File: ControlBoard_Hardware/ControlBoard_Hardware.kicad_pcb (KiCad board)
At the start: 2 copper layers, 141.5 x 46.2 mm, 24 parts, among them U2 TSR_1-2450

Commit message: updatedfor final report
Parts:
- added Conn13: Molex_SL_02, MRDT_Connectors:MOLEX_SL_02_Horizontal, F.Cu at (152.4, 68.6)
- Conn4: value Molex_SL_07 -> Molex_SL_02; footprint MRDT_Connectors:MOLEX_SL_07_Horizontal -> MRDT_Connectors:MOLEX_SL_02_Horizontal
- Conn5: value Molex_SL_07 -> Molex_SL_03; footprint MRDT_Connectors:MOLEX_SL_07_Horizontal -> MRDT_Connectors:MOLEX_SL_03_Horizontal
- moved Conn5 9.14 mm to (133.1, 68.6)
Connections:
- net Discharge2 renamed SERVO
- Conn10 pad 1: +5V -> +3V3
- Conn10 pad 2: +5V -> +3V3
- Conn11 pad 1: +5V -> +3V3
- Conn11 pad 2: +5V -> +3V3
- Conn12 pad 1: +5V -> +3V3
- Conn12 pad 2: +5V -> +3V3
- Conn3 pad 1: +5V -> +3V3
- Conn3 pad 2: +5V -> +3V3
- Conn4 pad 2: Charge2 -> Discharge1
- Conn5 pad 1: Discharge1 -> +5V
- Conn5 pad 3: Discharge3 -> GND
- Conn6 pad 1: +5V -> +3V3
- Conn6 pad 2: +5V -> +3V3
- Conn7 pad 1: +3V3 -> Trigger Signal
- Conn7 pad 2: Trigger Signal -> GND
- Conn8 pad 1: +5V -> +3V3
- Conn8 pad 2: +5V -> +3V3
- Conn9 pad 1: +5V -> +3V3
- Conn9 pad 2: +5V -> +3V3
- U1 pad 10: Discharge6 -> unconnected-(U1-CS-Pad10)
- U1 pad 11: Discharge7 -> unconnected-(U1-MOSI-Pad11)
- U1 pad 14: Charge2 -> unconnected-(U1-A0-Pad14)
- U1 pad 15: Charge3 -> unconnected-(U1-A1-Pad15)
- U1 pad 16: Charge4 -> unconnected-(U1-A2-Pad16)
- U1 pad 2: Charge5 -> unconnected-(U1-OUT2-Pad2)
- U1 pad 3: Charge6 -> unconnected-(U1-LRCLK2-Pad3)
- U1 pad 4: Charge7 -> unconnected-(U1-BCLK2-Pad4)
- U1 pad 7: Discharge3 -> unconnected-(U1-RX2-Pad7)
- U1 pad 8: Discharge4 -> unconnected-(U1-TX2-Pad8)
- U1 pad 9: Discharge5 -> unconnected-(U1-OUT1C-Pad9)
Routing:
- net +5V: track 77.4 -> 175.4 mm
- net Charge5: track 78.7 -> 0.00 mm
- net Charge6: track 73.1 -> 0.00 mm
- net Charge7: track 67.6 -> 0.00 mm
- net Charge3: track 62.7 -> 0.00 mm, vias 1 -> 0
- net Charge4: track 62.7 -> 0.00 mm, vias 1 -> 0
- net Charge2: track 62.7 -> 0.00 mm, vias 1 -> 0
- net +3V3: track 120.7 -> 60.0 mm, vias 0 -> 1
- net Discharge3: track 46.1 -> 0.00 mm
- net Discharge4: track 40.6 -> 0.00 mm
- net Discharge5: track 35.1 -> 0.00 mm
- net Discharge6: track 29.6 -> 0.00 mm
- net Discharge7: track 24.1 -> 0.00 mm
- net Discharge1: track 57.1 -> 75.0 mm
- net LCD_TX: track 118.1 -> 101.1 mm, vias 0 -> 1
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- added copper zone on F.Cu, net +3V3
- removed copper zone on F.Cu, net +5V
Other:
- board text added: "Charge/Discharge"
- board text added: "Safety Switch"
- board text added: "Servo"
- board text removed: "Charging Circuits"
- board text removed: "Discharge Circuits"

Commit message: started layout
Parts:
- removed D3: LED, LED_SMD:LED_0603_1608Metric_Pad1.05x0.95mm_HandSolder
- removed R3: 100, Resistor_SMD:R_0603_1608Metric_Pad0.98x0.95mm_HandSolder
- added Conn14: Molex_SL_02, MRDT_Connectors:MOLEX_SL_02_Horizontal, F.Cu at (215.9, 100.3)
- added PowerSwich1: Molex_SL_02, MRDT_Connectors:MOLEX_SL_02_Horizontal, F.Cu at (69.8, 100.3)
- Conn10, Conn11, Conn3, Conn6, Conn8, Conn9: value Molex_SL_05 -> Molex_SL_02; footprint MRDT_Connectors:MOLEX_SL_05_Horizontal -> MRDT_Connectors:MOLEX_SL_02_Horizontal
- Conn12: value Molex_SL_05 -> Molex_SL_03; footprint MRDT_Connectors:MOLEX_SL_05_Horizontal -> MRDT_Connectors:MOLEX_SL_03_Horizontal
- H1, H2, H3, H4: footprint MRDT_Drill_Holes:4_40_Hole_Corner -> MountingHole:MountingHole_3.2mm_M3
- moved H3 188.7 mm to (282.1, 43.1), turned to 0 degrees
- moved H2 184.1 mm to (282.1, 35.1), turned to 0 degrees
- moved Conn1 162.1 mm to (59.7, 100.3), turned to 0 degrees
- moved Conn4 111.3 mm to (226.1, 100.3)
- moved H1 87.2 mm to (282.1, 27.2), turned to 0 degrees
- moved Conn2 83.5 mm to (181.6, 100.3)
- moved D2 77.5 mm to (178.0, 127.0), turned to 0 degrees
- moved R2 76.3 mm to (182.3, 126.9), turned to 0 degrees
- moved U1 74.6 mm to (138.2, 124.8), turned to 0 degrees
- moved D1 73.2 mm to (178.0, 124.4), turned to 0 degrees
- moved R1 72.1 mm to (182.3, 124.4), turned to 0 degrees
- moved Conn11 69.0 mm to (134.6, 100.3), turned to 0 degrees
- moved U2 67.3 mm to (177.8, 118.1)
- moved Conn10 61.5 mm to (124.5, 100.3), turned to 0 degrees
- moved Conn9 54.0 mm to (114.3, 100.3), turned to 0 degrees
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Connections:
- net Charge1 renamed Charge
- Conn1 pad 2: Input_PWR -> Net-(Conn1-Pad2)
- Conn10 pad 1: +3V3 -> Coil5
- Conn10 pad 2: +3V3 -> GND
- Conn11 pad 1: +3V3 -> Coil6
- Conn11 pad 2: +3V3 -> GND
- Conn12 pad 1: +3V3 -> +5V
- Conn12 pad 2: +3V3 -> LED Data
- Conn12 pad 3: Sensor7 -> GND
- Conn3 pad 1: +3V3 -> Coil1
- Conn3 pad 2: +3V3 -> GND
- Conn4 pad 2: Discharge1 -> GND
- Conn6 pad 1: +3V3 -> Coil2
- Conn6 pad 2: +3V3 -> GND
- Conn8 pad 1: +3V3 -> Coil3
- Conn8 pad 2: +3V3 -> GND
- Conn9 pad 1: +3V3 -> Coil4
- Conn9 pad 2: +3V3 -> GND
- U1 pad 17: Sensor1 -> unconnected-(U1-A3-Pad17)
- U1 pad 18: Sensor2 -> Coil6
- U1 pad 19: Sensor3 -> Coil5
- U1 pad 20: Sensor4 -> Coil4
- U1 pad 21: Sensor5 -> Coil3
- U1 pad 22: Sensor6 -> Coil2
- U1 pad 23: Sensor7 -> Coil1
- U1 pad 5: Discharge1 -> Discharge
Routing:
- net +5V: track 175.4 -> 0.00 mm
- net LCD_TX: track 101.1 -> 0.00 mm, vias 1 -> 0
- net LCD_RX: track 100.5 -> 0.00 mm
- net Sensor1: track 80.8 -> 0.00 mm
- net Discharge1: track 75.0 -> 0.00 mm
- net Sensor2: track 65.6 -> 0.00 mm
- net Charge: track 65.2 -> 0.00 mm, vias 1 -> 0
- net +3V3: track 60.0 -> 0.00 mm, vias 1 -> 0
- net SERVO: track 58.3 -> 0.00 mm
- net Sensor3: track 51.0 -> 0.00 mm
- net Sensor4: track 35.1 -> 0.00 mm
- net Input_PWR: track 25.7 -> 0.00 mm
- net Sensor5: track 19.9 -> 0.00 mm
- net Sensor7: track 16.1 -> 0.00 mm
- net Trigger Signal: track 13.3 -> 0.00 mm
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- removed copper zone on F.Cu, net +3V3
- removed copper zone on B.Cu, net GND
- removed copper zone on F.Cu, net GND
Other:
- board outline removed
- board text removed: "Charge/Discharge"
- board text removed: "Control Board, Rev1 Kinetic Antenna Missouri S&T, 23-24"
- board text removed: "LCD"
- board text removed: "Safety Switch"
- board text removed: "Sensor 1"
- board text removed: "Sensor 2"
- board text removed: "Sensor 3"
- board text removed: "Sensor 4"
- board text removed: "Sensor 5"
- board text removed: "Sensor 6"
- board text removed: "Sensor 7"
- board text removed: "Servo"
- board text removed: "Trigger"

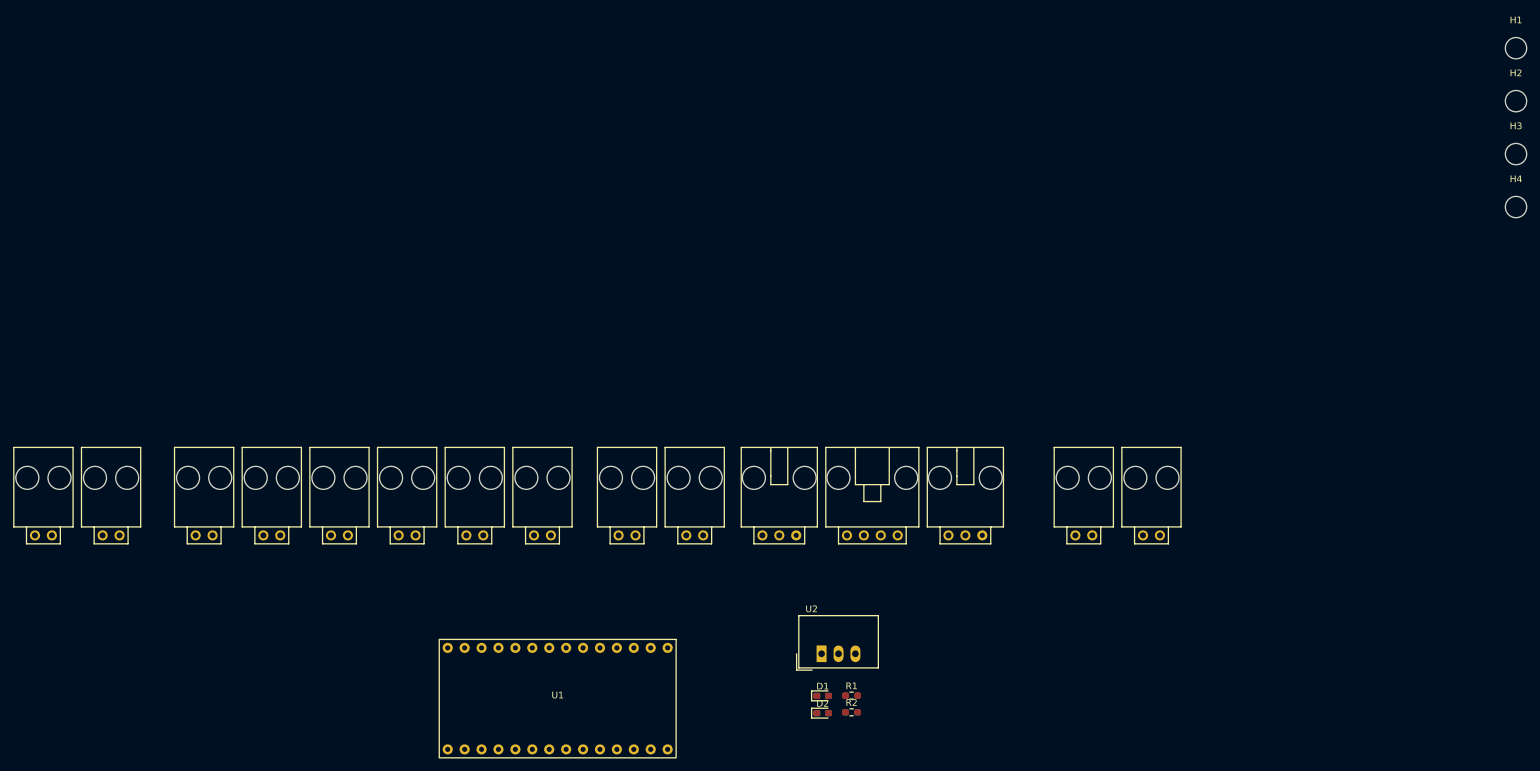
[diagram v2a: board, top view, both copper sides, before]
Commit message: Started layout
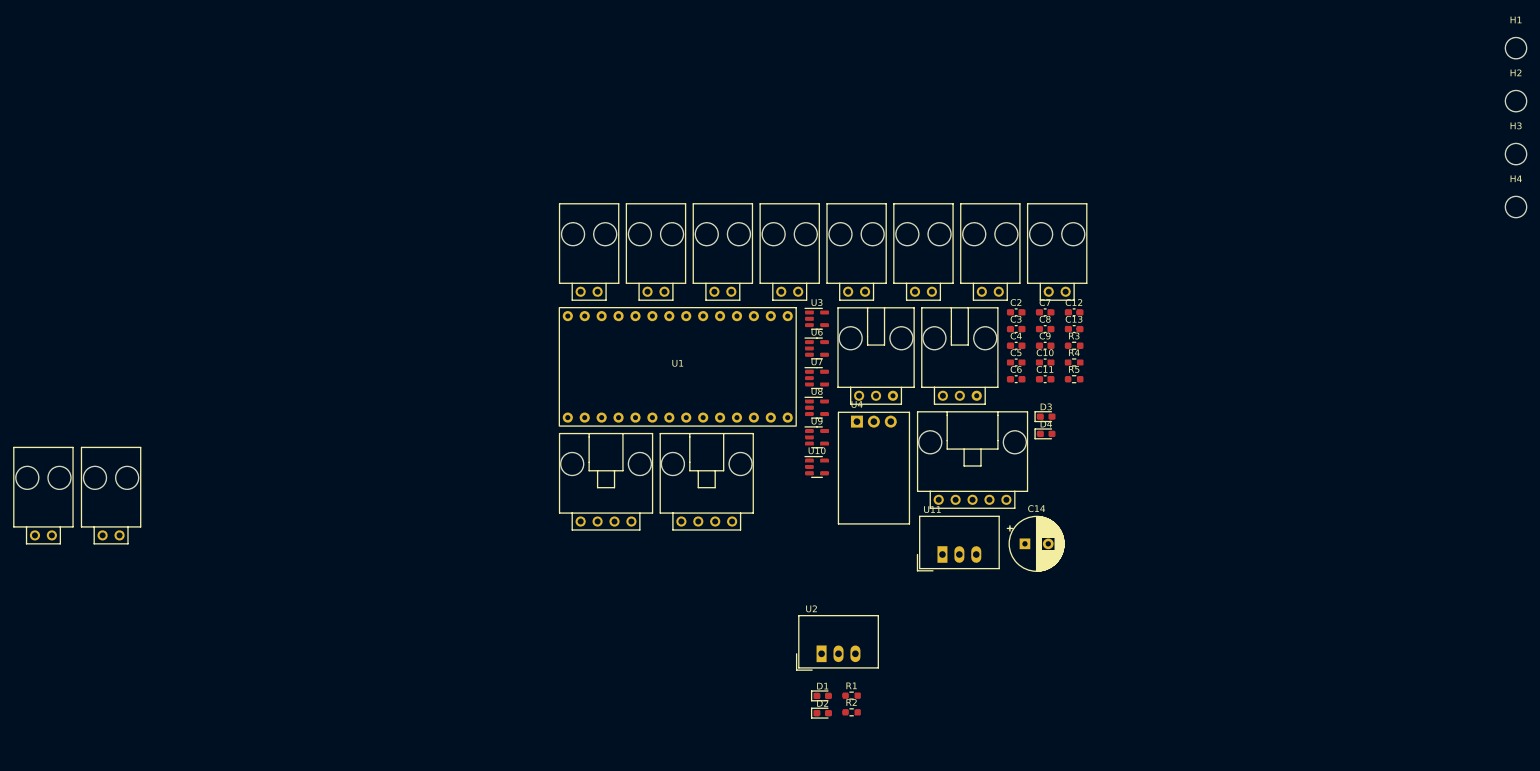
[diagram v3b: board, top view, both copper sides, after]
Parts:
- added C10: 10uF, Capacitor_SMD:C_0603_1608Metric_Pad1.08x0.95mm_HandSolder, F.Cu at (211.4, 74.4)
- added C11: 0.1uF, Capacitor_SMD:C_0603_1608Metric_Pad1.08x0.95mm_HandSolder, F.Cu at (211.4, 76.9)
- added C12: 10uF, Capacitor_SMD:C_0603_1608Metric_Pad1.08x0.95mm_HandSolder, F.Cu at (215.7, 66.8)
- added C13: 0.1uF, Capacitor_SMD:C_0603_1608Metric_Pad1.08x0.95mm_HandSolder, F.Cu at (215.7, 69.3)
- added C14: 1000uF, Capacitor_THT:CP_Radial_D8.0mm_P3.50mm, F.Cu at (208.3, 101.6)
- added C2: 10uF, Capacitor_SMD:C_0603_1608Metric_Pad1.08x0.95mm_HandSolder, F.Cu at (207.0, 66.8)
- added C3: 0.1uF, Capacitor_SMD:C_0603_1608Metric_Pad1.08x0.95mm_HandSolder, F.Cu at (207.0, 69.3)
- added C4: 10uF, Capacitor_SMD:C_0603_1608Metric_Pad1.08x0.95mm_HandSolder, F.Cu at (207.0, 71.9)
- added C5: 0.1uF, Capacitor_SMD:C_0603_1608Metric_Pad1.08x0.95mm_HandSolder, F.Cu at (207.0, 74.4)
- added C6: 10uF, Capacitor_SMD:C_0603_1608Metric_Pad1.08x0.95mm_HandSolder, F.Cu at (207.0, 76.9)
- added C7: 0.1uF, Capacitor_SMD:C_0603_1608Metric_Pad1.08x0.95mm_HandSolder, F.Cu at (211.4, 66.8)
- added C8: 10uF, Capacitor_SMD:C_0603_1608Metric_Pad1.08x0.95mm_HandSolder, F.Cu at (211.4, 69.3)
- added C9: 0.1uF, Capacitor_SMD:C_0603_1608Metric_Pad1.08x0.95mm_HandSolder, F.Cu at (211.4, 71.9)
- added D3: LED, LED_SMD:LED_0603_1608Metric_Pad1.05x0.95mm_HandSolder, F.Cu at (211.5, 82.5)
- added D4: LED, LED_SMD:LED_0603_1608Metric_Pad1.05x0.95mm_HandSolder, F.Cu at (211.5, 85.1)
- added R3: 1000, Resistor_SMD:R_0603_1608Metric_Pad0.98x0.95mm_HandSolder, F.Cu at (215.7, 71.9)
- added R4: 120, Resistor_SMD:R_0603_1608Metric_Pad0.98x0.95mm_HandSolder, F.Cu at (215.7, 74.4)
- added R5: 300, Resistor_SMD:R_0603_1608Metric_Pad0.98x0.95mm_HandSolder, F.Cu at (215.7, 76.9)
- added U10: MCP1415, Package_TO_SOT_SMD:SOT-23-5, F.Cu at (177.1, 90.1)
- added U11: TSR_1-2450, Converter_DCDC:Converter_DCDC_TRACO_TSR-1_THT, F.Cu at (195.9, 103.2)
- added U3: MCP1415, Package_TO_SOT_SMD:SOT-23-5, F.Cu at (177.1, 67.8)
- added U4: OKI-78SR-12, Converter_DCDC:Converter_DCDC_Murata_OKI-78SR_Horizontal, F.Cu at (183.1, 83.2)
- added U6: MCP1415, Package_TO_SOT_SMD:SOT-23-5, F.Cu at (177.1, 72.3)
- added U7: MCP1415, Package_TO_SOT_SMD:SOT-23-5, F.Cu at (177.1, 76.7)
- added U8: MCP1415, Package_TO_SOT_SMD:SOT-23-5, F.Cu at (177.1, 81.2)
- added U9: MCP1415, Package_TO_SOT_SMD:SOT-23-5, F.Cu at (177.1, 85.6)
- Conn3: value Molex_SL_02 -> Molex_SL_05; footprint MRDT_Connectors:MOLEX_SL_02_Horizontal -> MRDT_Connectors:MOLEX_SL_05_Horizontal
- Conn4: value Molex_SL_02 -> Molex_SL_04; footprint MRDT_Connectors:MOLEX_SL_02_Horizontal -> MRDT_Connectors:MOLEX_SL_04_Horizontal
- moved Conn3 111.7 mm to (195.4, 95.0)
- moved Conn4 69.3 mm to (156.7, 98.2)
- moved Conn8 68.2 mm to (161.7, 63.7)
- moved Conn9 68.1 mm to (171.7, 63.7)
- moved Conn10 68.0 mm to (181.8, 63.7)
- moved Conn11 67.9 mm to (191.8, 63.7)
- moved Conn6 60.1 mm to (141.6, 63.7)
- moved Conn13 57.5 mm to (201.9, 63.7)
- moved U1 53.0 mm to (156.2, 75.0)
- moved Conn2 40.0 mm to (141.6, 98.2)
- moved Conn7 36.8 mm to (151.7, 63.7)
- moved Conn14 36.8 mm to (211.9, 63.7)
- moved Conn5 25.5 mm to (183.4, 79.4)
- moved Conn12 21.0 mm to (196.0, 79.4)
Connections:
- Conn10 pad 1: Coil5 -> COIL_4_T
- Conn11 pad 1: Coil6 -> COIL_5_T
- Conn12 pad 1: +5V -> +5VA
- Conn12 pad 2: LED Data -> Net-(Conn12-Pad2)
- Conn14 pad 1: Discharge -> COIL_6_T
- Conn3 pad 1: Coil1 -> +3.3V
- Conn3 pad 2: GND -> Voltage_Sens
- Conn4 pad 1: Charge -> Charge_Toggle
- Conn4 pad 2: GND -> FAULT
- Conn6 pad 1: Coil2 -> COIL_1_T
- Conn8 pad 1: Coil3 -> COIL_2_T
- Conn9 pad 1: Coil4 -> COIL_3_T
- PowerSwich1 pad 2: Input_PWR -> /PWR_IN
- U1 pad 0: LCD_TX -> LCD_RX
- U1 pad 1: LCD_RX -> LCD_TX
- U1 pad 11: unconnected-(U1-MOSI-Pad11) -> Relay_Toggle
- U1 pad 12: Trigger Signal -> Discharge_Toggle
- U1 pad 13: Charge -> unconnected-(U1-SCK-Pad13)
- U1 pad 14: unconnected-(U1-A0-Pad14) -> Voltage_Sens
- U1 pad 15: unconnected-(U1-A1-Pad15) -> Trigger Signal
- U1 pad 16: unconnected-(U1-A2-Pad16) -> Safety Switch
- U1 pad 17: unconnected-(U1-A3-Pad17) -> COIL_6_L
- U1 pad 18: Coil6 -> COIL_5_L
- U1 pad 19: Coil5 -> COIL_4_L
- U1 pad 2: unconnected-(U1-OUT2-Pad2) -> Charge_Toggle
- U1 pad 20: Coil4 -> COIL_3_L
- U1 pad 21: Coil3 -> COIL_2_L
- U1 pad 22: Coil2 -> COIL_1_L
- U1 pad 23: Coil1 -> unconnected-(U1-A9-Pad23)
- U1 pad 3: unconnected-(U1-LRCLK2-Pad3) -> FAULT
- U1 pad 4: unconnected-(U1-BCLK2-Pad4) -> DONE
- U1 pad 5: Discharge -> unconnected-(U1-IN2-Pad5)
- U1 pad 6: SERVO -> unconnected-(U1-OUT1D-Pad6)
- U1 pad 7: unconnected-(U1-RX2-Pad7) -> LED Data
- U1 pad 8: unconnected-(U1-TX2-Pad8) -> SERVO
- U2 pad 1: Input_PWR -> /PWR_IN

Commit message: finished board layour
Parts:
- removed H4: MountingHole, MountingHole:MountingHole_3.2mm_M3
- added D5: LED, LED_SMD:LED_0603_1608Metric_Pad1.05x0.95mm_HandSolder, F.Cu at (158.8, 87.1)
- added R6: 300, Resistor_SMD:R_0603_1608Metric_Pad0.98x0.95mm_HandSolder, F.Cu at (162.6, 87.1)
- moved H3 171.1 mm to (120.1, 98.3)
- moved H2 95.8 mm to (210.1, 98.3)
- moved Conn1 77.7 mm to (136.4, 88.3), turned to 180 degrees
- moved PowerSwich1 77.4 mm to (146.3, 88.3), turned to 180 degrees
- moved H1 73.0 mm to (210.1, 38.9)
- moved Conn13 72.6 mm to (130.8, 48.9)
- moved Conn3 71.3 mm to (130.2, 66.0), turned to 90 degrees
- moved C12 70.5 mm to (146.6, 53.2), turned to 90 degrees
- moved C13 69.3 mm to (148.3, 53.2), turned to 90 degrees
- moved Conn2 60.5 mm to (200.0, 82.5), turned to -90 degrees
- moved C10 58.5 mm to (156.7, 53.5), turned to 90 degrees
- moved C11 57.8 mm to (158.5, 53.5), turned to 90 degrees
- moved R3 57.5 mm to (162.6, 93.7), turned to 180 degrees
- moved R4 54.0 mm to (162.6, 83.8), turned to 180 degrees
- moved D3 53.9 mm to (158.8, 93.7)
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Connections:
- Conn3 pad 1: +3.3V -> +3V3
- R1 pad 1: Input_PWR -> /PWR_IN
- R4 pad 1: +3.3V -> +3V3
- U1 pad 11: Relay_Toggle -> Discharge_Toggle
- U1 pad 12: Discharge_Toggle -> Relay_Toggle
- U1 pad 15: Trigger Signal -> Safety Switch
- U1 pad 16: Safety Switch -> Trigger Signal
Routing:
- net +12V: track 0.00 -> 219.3 mm, vias 0 -> 4
- net +5V: track 0.00 -> 134.5 mm, vias 0 -> 3
- net +5VA: track 0.00 -> 104.7 mm
- net /PWR_IN: track 0.00 -> 78.6 mm, vias 0 -> 1
- net LCD_RX: track 0.00 -> 57.8 mm, vias 0 -> 1
- net LCD_TX: track 0.00 -> 57.3 mm, vias 0 -> 1
- net Trigger Signal: track 0.00 -> 53.3 mm
- net Relay_Toggle: track 0.00 -> 52.7 mm, vias 0 -> 1
- net Discharge_Toggle: track 0.00 -> 51.2 mm, vias 0 -> 1
- net +3V3: track 0.00 -> 49.5 mm, vias 0 -> 1
- net Safety Switch: track 0.00 -> 45.6 mm
- net Voltage_Sens: track 0.00 -> 44.9 mm
- net LED Data: track 0.00 -> 39.8 mm
- net SERVO: track 0.00 -> 35.3 mm
- net COIL_6_L: track 0.00 -> 32.8 mm, vias 0 -> 1
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- added copper zone on B.Cu, net GND
- added copper zone on F.Cu, net GND
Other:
- board outline added: 96.5 x 66 mm
